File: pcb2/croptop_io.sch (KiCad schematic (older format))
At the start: 162 parts, among them J10 1702474, J11 1702474, J12 1702474, J13 1702474, J14 1702474, J7 1702474, J8 1702474, J9 1702474, Q3 FDMA530PZ, U18 AP22802AW5, U19 74HCT125D653, U20 AP22802AW5, U21 AD7799, U22 TPD4E1U06DBV, U23 AP22802AW5, U24 TPD4E1U06DBV, U25 TPD4E1U06DBV, U26 TPD4E1U06DBV, U27 DRV8872, U28 DRV8825, U29 AP22802AW5

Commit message: Footprints done, board started
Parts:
- removed D13, D14, D17, D19: LTSTC171GKT, LED_SMD:LED_0805_2012Metric, symbol Device:LED
- removed JP1: N.0., symbol Jumper:SolderJumper_2_Open
- removed Q3: FDMA530PZ, symbol Device:Q_PMOS_DGS
- removed R100, R94, R95, R96: 110m, symbol Device:R
- removed R60, R68, R73, R93: 10k, Resistor_SMD:R_0402_1005Metric, symbol Device:R
- removed R70, R72, R99: 100, Resistor_SMD:R_0402_1005Metric, symbol Device:R
- removed R71: 0, Resistor_SMD:R_0402_1005Metric, symbol Device:R
- removed R75: 220, Resistor_SMD:R_0402_1005Metric, symbol Device:R
- removed TP59, TP60, TP63, TP95: TestPoint, symbol Connector:TestPoint
- added C74, C76: 0.1u, Capacitor_SMD:C_0402_1005Metric, symbol Device:C
- added JP1: Solder Jumper, Jumper:SolderJumper-3_P1.3mm_Bridged12_RoundedPad1.0x1.5mm, symbol Jumper:SolderJumper_3_Bridged12
- added Q3: Q2319ADS-T1-GE3, Package_TO_SOT_SMD:SOT-23, symbol Device:Q_PMOS_GSD
- added R83, R84, R88: 0.2, Resistor_SMD:R_2512_6332Metric, symbol Device:R
- C45: renamed from C46; footprint Capacitor_SMD:C_0402_1005Metric -> Capacitor_SMD:C_1206_3216Metric
- C46: renamed from C47; footprint Capacitor_SMD:C_0402_1005Metric -> Capacitor_SMD:C_1206_3216Metric
- C47: renamed from C45; footprint Capacitor_SMD:C_0402_1005Metric -> Capacitor_SMD:C_1206_3216Metric
- C48, C51, C52, C56, C58, C61, C62: footprint Capacitor_SMD:C_0402_1005Metric -> Capacitor_SMD:C_1206_3216Metric
- C66: renamed from C67; value 0.1u -> 0.01u; MPN (none) -> CL05B103KB5NNNC; Rating (none) -> 50V
- C67: renamed from C66; footprint Capacitor_SMD:C_0402_1005Metric -> Capacitor_SMD:C_1206_3216Metric
- C68, C71: footprint Capacitor_SMD:C_0402_1005Metric -> Capacitor_SMD:C_0805_2012Metric; Rating (none) -> 50V
- C69: renamed from C70; Rating (none) -> 50V
- C70: renamed from C69; footprint Capacitor_SMD:C_0402_1005Metric -> Capacitor_SMD:C_0805_2012Metric
- C72: Rating (none) -> 35V
- C75: renamed from C74; footprint Capacitor_SMD:C_0402_1005Metric -> Capacitor_SMD:C_1206_3216Metric
- D12: renamed from D15; footprint (none) -> Diode_SMD:D_0201_0603Metric
- D13: renamed from D16; footprint (none) -> Diode_SMD:D_0201_0603Metric
- D14: renamed from D18; footprint (none) -> Diode_SMD:D_0201_0603Metric
- D15: renamed from D20; footprint (none) -> Diode_SMD:D_SMA
- D16: renamed from D21; footprint (none) -> Diode_SMD:D_0201_0603Metric
- D17: renamed from D22; footprint (none) -> Package_TO_SOT_SMD:SOT-323_SC-70
- D18: renamed from D23; footprint (none) -> Package_TO_SOT_SMD:SOT-323_SC-70
- D19: renamed from D24; footprint (none) -> Package_TO_SOT_SMD:SOT-323_SC-70
- D20: renamed from D25; footprint (none) -> Package_TO_SOT_SMD:SOT-323_SC-70
- J10, J11, J12, J13, J14, J7, J8, J9: footprint (none) -> croptop:solderless_terminal
- L4: footprint (none) -> Inductor_SMD:L_0402_1005Metric
- R85: renamed from R98; footprint (none) -> Resistor_SMD:R_0402_1005Metric
- R89: renamed from R101; value 110m -> 0.2; footprint (none) -> Resistor_SMD:R_2512_6332Metric; MPN (none) -> CSRN2512FKR200
- TP50: renamed from TP53; footprint (none) -> croptop:TestPoint
- TP51: renamed from TP54; footprint (none) -> croptop:TestPoint
- TP52: renamed from TP55; footprint (none) -> croptop:TestPoint
- TP53: renamed from TP56; footprint (none) -> croptop:TestPoint
- TP54: renamed from TP57; footprint (none) -> croptop:TestPoint
- TP55: renamed from TP58; footprint (none) -> croptop:TestPoint
- TP56: renamed from TP61; footprint (none) -> croptop:TestPoint
- TP58: renamed from TP64; footprint (none) -> croptop:TestPoint
- TP59: renamed from TP65; footprint (none) -> croptop:TestPoint
- TP60: renamed from TP66; footprint (none) -> croptop:TestPoint
- TP61: renamed from TP67; footprint (none) -> croptop:TestPoint
- TP62: renamed from TP68; footprint (none) -> croptop:TestPoint
- TP63: renamed from TP69; footprint (none) -> croptop:TestPoint
- TP64: renamed from TP70; footprint (none) -> croptop:TestPoint
- TP65: renamed from TP71; footprint (none) -> croptop:TestPoint
- TP66: renamed from TP72; footprint (none) -> croptop:TestPoint
- TP67: renamed from TP73; footprint (none) -> croptop:TestPoint
- TP68: renamed from TP62; footprint (none) -> croptop:TestPoint
- TP69: renamed from TP74; footprint (none) -> croptop:TestPoint
- TP70: renamed from TP75; footprint (none) -> croptop:TestPoint
- TP71: renamed from TP76; footprint (none) -> croptop:TestPoint
- TP72: renamed from TP77; footprint (none) -> croptop:TestPoint
- TP73: renamed from TP78; footprint (none) -> croptop:TestPoint
- TP74: renamed from TP79; footprint (none) -> croptop:TestPoint
- TP75: renamed from TP80; footprint (none) -> croptop:TestPoint
- TP76: renamed from TP81; footprint (none) -> croptop:TestPoint
- TP77: renamed from TP82; footprint (none) -> croptop:TestPoint
- TP78: renamed from TP83; footprint (none) -> croptop:TestPoint
- TP79: renamed from TP84; footprint (none) -> croptop:TestPoint
- TP80: renamed from TP85; footprint (none) -> croptop:TestPoint
- TP81: renamed from TP86; footprint (none) -> croptop:TestPoint
- TP82: renamed from TP87; footprint (none) -> croptop:TestPoint
- TP83: renamed from TP88; footprint (none) -> croptop:TestPoint
- TP84: renamed from TP89; footprint (none) -> croptop:TestPoint
- TP85: renamed from TP90; footprint (none) -> croptop:TestPoint
- TP86: renamed from TP91; footprint (none) -> croptop:TestPoint
- TP87: renamed from TP92; footprint (none) -> croptop:TestPoint
- TP88: renamed from TP93; footprint (none) -> croptop:TestPoint
- TP89: renamed from TP94; footprint (none) -> croptop:TestPoint
- TP90: renamed from TP96; footprint (none) -> croptop:TestPoint
- TP91: renamed from TP97; footprint (none) -> croptop:TestPoint
- TP92: renamed from TP98; footprint (none) -> croptop:TestPoint
- TP93: renamed from TP100; footprint (none) -> croptop:TestPoint
- TP94: renamed from TP99; footprint (none) -> croptop:TestPoint
- TP95: renamed from TP101; footprint (none) -> croptop:TestPoint
- TP96: renamed from TP102; footprint (none) -> croptop:TestPoint
- TP97: renamed from TP103; footprint (none) -> croptop:TestPoint
- TP98: renamed from TP104; footprint (none) -> croptop:TestPoint
- U19: renamed from U18; footprint (none) -> Package_TO_SOT_SMD:SOT-23-5
- U21: renamed from U20; footprint (none) -> Package_TO_SOT_SMD:SOT-23-5
- U23, U29: footprint (none) -> Package_TO_SOT_SMD:SOT-23-5
- renumbered C75 to C77, R61 to R55, R62 to R56, R64 to R57, R65 to R58, R66 to R59, R67 to R60, R63 to R61, R69 to R62, R74 to R65, R76 to R66, R77 to R67, R78 to R68, R79 to R69, R80 to R70, R81 to R71, R82 to R72, R83 to R73, R84 to R74, R85 to R75, R86 to R76, R87 to R77, R88 to R78, R89 to R79, R90 to R80, R91 to R81, R92 to R82, R97 to R86, R102 to R87, U19 to U18, U21 to U20
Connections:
- net ~ENCDR_PWR_FAULT is gone; now on net ~PWR_FAULT: U23.3 (FLG)
- net ~POTEN_PWR_FAULT is gone; now on net ~PWR_FAULT: U19.3 (FLG)
- net ~SONIC_PWR_FAULT is gone; now on net ~PWR_FAULT: U21.3 (FLG)
- net +3V3: now also JP1.3 (B)
- net +5V: now also JP1.1 (A)
- net DGND: now also C74.2, C76.2, R83.2, R84.2, R88.2
- net at C68.1, C69.2, C70.1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: now also Q3.2 (S)
- net at U27.7 (ISEN): now also R83.1, R84.1
- net at C73.1, U28.12 (AVREF), U28.13 (BVREF)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: now also C74.1, C76.1
- net at U28.9 (ISENB): now also R88.1
- net at C51.1, R65.1, U23.4 (EN)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: now also JP1.2 (C)
- net at D18.1 (A1), D18.2 (A2), J13.3 (Pin_3): now also Q3.3 (D)
- net at D15.2 (A), R87.1: now also Q3.1 (G)
- net ~ADI_PWR_FAULT renamed ~PWR_FAULT
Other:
- note added: "Scratch 1-2 connection\nand solder 3-2 connection\nfor 3.3V encoders"
- note removed: "RL1220S-R11"
- note removed: "Remove resistor \nif using jumper"
- moved on the sheet: C47, C48, C67, C70, C71, C73, R61, R62, R86, R89, TP56, TP68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

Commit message: Updated prez
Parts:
- U18: footprint (none) -> Package_SO:SOIC-14_3.9x8.7mm_P1.27mm
- U22, U24, U25, U26: footprint (none) -> Package_TO_SOT_SMD:SOT-23-6
- U28: footprint (none) -> Package_SO:HTSSOP-28-1EP_4.4x9.7mm_P0.65mm_EP3.4x9.5mm_Mask2.4x6.17mm_ThermalVias
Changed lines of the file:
@@
 F 0 "U25" H 8850 3426 50  0000 C CNN
 F 1 "TPD4E1U06DBV" H 8850 3335 50  0000 C CNN
-F 2 "" V 9100 3100 50  0001 C CNN
+F 2 "Package_TO_SOT_SMD:SOT-23-6" V 9100 3100 50  0001 C CNN
 F 3 "http://www.ti.com/lit/ds/symlink/tpd4e1u06.pdf" V 9100 3100 50  0001 C CNN
 	1    8850 3650
@@
 F 0 "U26" H 9750 3426 50  0000 C CNN
 F 1 "TPD4E1U06DBV" H 9750 3335 50  0000 C CNN
-F 2 "" V 10000 3100 50  0001 C CNN
+F 2 "Package_TO_SOT_SMD:SOT-23-6" V 10000 3100 50  0001 C CNN
 F 3 "http://www.ti.com/lit/ds/symlink/tpd4e1u06.pdf" V 10000 3100 50  0001 C CNN
 	1    9750 3650
@@
 F 0 "U18" H 2150 9500 50  0000 C CNN
 F 1 "74HCT125D653" H 2150 9400 50  0000 C CNN
-F 2 "" H 3500 9250 50  0001 C CNN
+F 2 "Package_SO:SOIC-14_3.9x8.7mm_P1.27mm" H 3500 9250 50  0001 C CNN
 F 3 "https://assets.nexperia.com/documents/data-sheet/74HC_HCT125.pdf" H 3500 9250 50  0001 C CNN
 	1    2450 9250
@@
 F 0 "U22" H 3550 9726 50  0000 C CNN
 F 1 "TPD4E1U06DBV" H 3550 9635 50  0000 C CNN
-F 2 "" V 3800 9400 50  0001 C CNN
+F 2 "Package_TO_SOT_SMD:SOT-23-6" V 3800 9400 50  0001 C CNN
 F 3 "http://www.ti.com/lit/ds/symlink/tpd4e1u06.pdf" V 3800 9400 50  0001 C CNN
 	1    3550 9950
@@
 F 0 "U28" H 11400 8800 50  0000 C CNN
 F 1 "DRV8825" H 11400 8700 50  0000 C CNN
-F 2 "" H 11150 8550 50  0001 C CNN
+F 2 "Package_SO:HTSSOP-28-1EP_4.4x9.7mm_P0.65mm_EP3.4x9.5mm_Mask2.4x6.17mm_ThermalVias" H 11150 8550 50  0001 C CNN
 F 3 "http://www.ti.com/lit/ds/symlink/drv8825.pdf" H 11150 8550 50  0001 C CNN
 	1    11150 8050
@@
 F 0 "U24" H 6350 7376 50  0000 C CNN
 F 1 "TPD4E1U06DBV" H 6350 7285 50  0000 C CNN
-F 2 "" V 6600 7050 50  0001 C CNN
+F 2 "Package_TO_SOT_SMD:SOT-23-6" V 6600 7050 50  0001 C CNN
 F 3 "http://www.ti.com/lit/ds/symlink/tpd4e1u06.pdf" V 6600 7050 50  0001 C CNN
 	1    6350 7600

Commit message: Board almost done
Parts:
- removed TP70, TP71, TP73, TP77, TP79, TP83: TestPoint, croptop:TestPoint, symbol Connector:TestPoint
- renumbered C67 to C66, C66 to C67, C75 to C72, C72 to C73, C73 to C74, C77 to C75, C74 to C76, C76 to C77, R65 to R63, R66 to R64, R67 to R65, R68 to R66, R69 to R67, R70 to R68, R71 to R69, R72 to R70, R73 to R71, R74 to R72, R75 to R73, R76 to R74, R77 to R75, R78 to R76, R79 to R77, R80 to R78, R81 to R79, R82 to R80, R86 to R81, R83 to R82, R84 to R83, R85 to R84, R87 to R85, R88 to R86, R89 to R87, TP50 to TP16, TP51 to TP17, TP52 to TP18, TP53 to TP19, TP54 to TP20, TP55 to TP21, TP56 to TP22, TP58 to TP23, TP59 to TP24, TP60 to TP25, TP61 to TP26, TP62 to TP27, TP63 to TP28, TP64 to TP29, TP65 to TP30, TP66 to TP31, TP67 to TP32, TP68 to TP33, TP69 to TP34, TP72 to TP35, TP74 to TP36, TP75 to TP37, TP76 to TP38, TP78 to TP39, TP80 to TP40, TP81 to TP41, TP82 to TP42, TP84 to TP43, TP85 to TP44, TP86 to TP45, TP87 to TP46, TP88 to TP47, TP89 to TP48, TP90 to TP49, TP91 to TP50, TP92 to TP51, TP94 to TP52, TP93 to TP53, TP95 to TP54, TP96 to TP55, TP97 to TP56, TP98 to TP57
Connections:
- net ENCDR_A: now also R56.2, TP16.1; no longer R55.2, TP17.1
- net ENCDR_B: now also R55.2, TP17.1; no longer R56.2, TP16.1
- net at D17.2 (A2), TP51.1, U27.6 (OUT1): now also J13.2 (Pin_2); no longer J13.1 (Pin_1)
- net at D17.1 (A1), TP50.1, U27.8 (OUT2): now also J13.1 (Pin_1); no longer J13.2 (Pin_2)
- net at R64.2, U22.6 (D1-): now also U18.5 (A2); no longer U18.2 (A1)
- net at R65.2, U22.1 (D1+): now also U18.2 (A1); no longer U18.5 (A2)
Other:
- moved on the sheet: C66, C72, C75, D16, J10, J11, J12, R81, TP52, U29

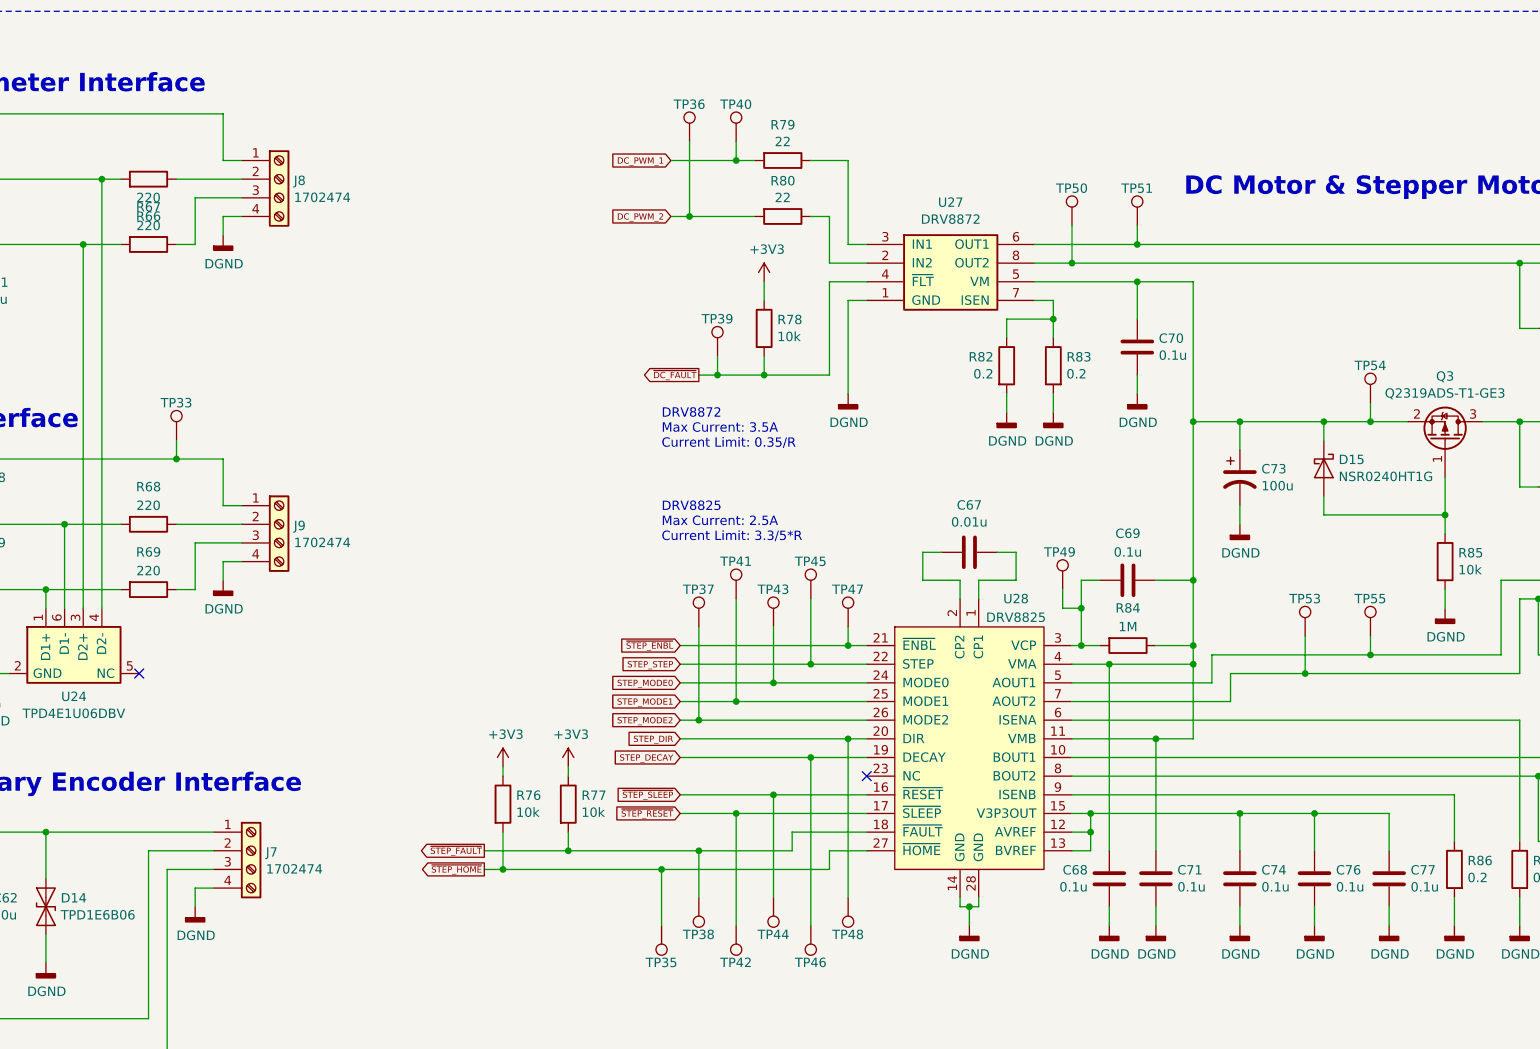
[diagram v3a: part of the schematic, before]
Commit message: Updated PCB2, Changed MotorLib, Changed PotLib
- Updated PCB2 to have all correct MPNs
- Added some useful macros within the standard hardware heade file
- Changed hardware initialization function calls (for main, MotorLib, and PotLib) to return an error flag.
- Corrected GPIO configurations for switches, LEDS
- Made initialize_system() private
- Added Doxygen to MotorLib and PotLib files
- Reduced bloat of MotorLib by combining subsystem setup functions into one.
- Added boundary condition checks for PWM functions
- Added error-flag return values to motor functions
- Corrected issue where CN14 was "used" to detect faults, but in PCBv2.2 CN14 is connected to GPU_INT, and INT1 is connected to DC_FAULT. Updated code accordingly.
- Made ADC / Potentiometer functionality "smart" configure T3 to sample the ADC at a variable, desired frequency.
- Updated potentiometer configuration to use AN9 and AN10
- Added error-flag returns to initialize_potentiometer()
- Added ISR for timer 3 that is used to trigger ADC samples automatically
- Added multi-inclusion protection to all currently-addressed files (will do rest later)

** THIS HAS NOT BEEN COMPILE VERIFIED - CHECK WITH XC32 COMPILER **
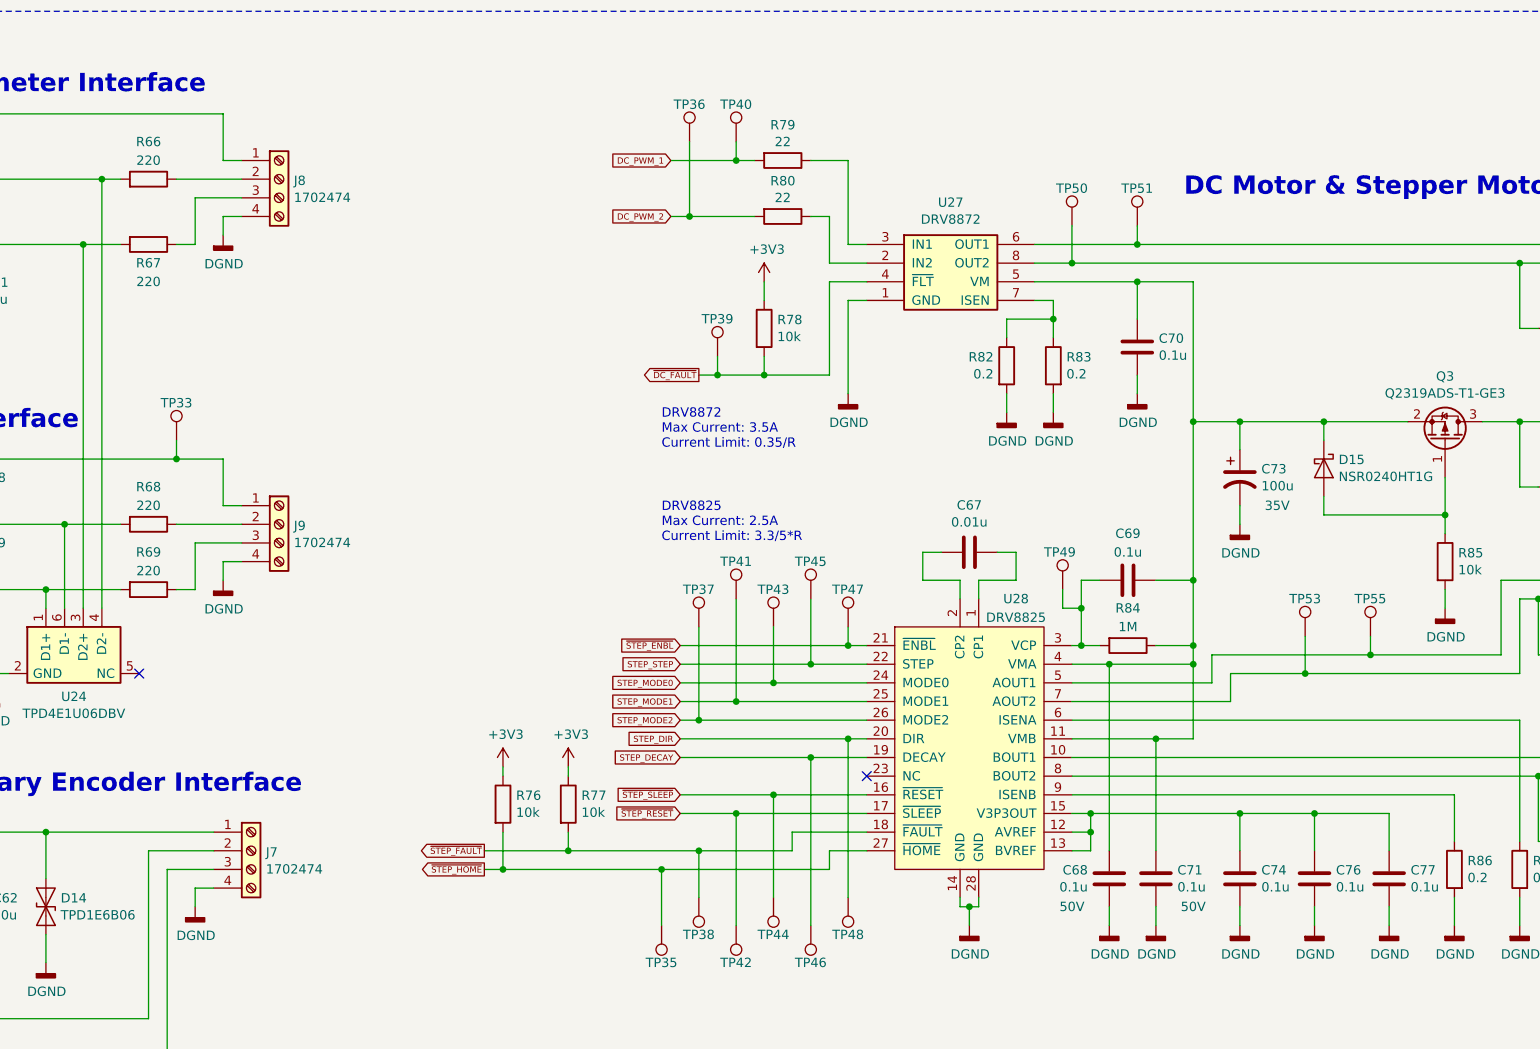
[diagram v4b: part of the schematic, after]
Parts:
- removed TP54: TestPoint, croptop:TestPoint, symbol Connector:TestPoint
- C45, C46, C47, C48, C51, C52, C56, C58, C61, C62, C66, C72: MPN (none) -> CC1206ZRY5V6BB106
- C49, C50, C53, C54, C55, C57, C59, C60, C63, C64, C65, C69, C74, C75, C76, C77: MPN (none) -> CL05F104ZO5NNNC
- C67: MPN CL05B103KB5NNNC -> CC0402KRX7R9BB103
- C68, C70, C71: MPN (none) -> C0805C104Z5VACTU
- C73: MPN (none) -> UWT1V101MCL1GS
- D12, D13, D14, D16: MPN (none) -> TPD1E6B06DPLR
- D15: footprint Diode_SMD:D_SMA -> Diode_SMD:D_SOD-323; MPN (none) -> NSR0240HT1G
- D17, D18, D19, D20: MPN (none) -> TPD2E007DCKR
- J10, J11, J12, J13, J14, J7, J8, J9: MPN (none) -> 277-2338-1-ND
- JP1: MPN (none) -> JL-100-25-T
- L4: MPN (none) -> BKP1005HS121-TV
- Q3: MPN (none) -> SQ2319ADS-T1_GE3
- R55, R56, R57, R58, R59, R60, R79, R80: MPN (none) -> RC0402FR-0722RL
- R61, R62, R63, R76, R77, R78, R81, R85: MPN (none) -> RC0402FR-0710KL
- R64, R65, R66, R67, R68, R69: MPN (none) -> CRGCQ0402F220R
- R70, R71, R72, R73, R74, R75: MPN (none) -> RC0402FR-07100RL
- R84: MPN (none) -> RC0402FR-071ML
- TP16, TP17, TP18, TP19, TP20, TP21, TP22, TP23, TP24, TP25, TP26, TP27, TP28, TP29, TP30, TP31, TP32, TP33, TP34, TP35, TP36, TP37, TP38, TP39, TP40, TP41, TP42, TP43, TP44, TP45, TP46, TP47, TP48, TP49, TP50, TP51, TP52, TP53, TP55, TP56, TP57: footprint croptop:TestPoint -> TestPoint:TestPoint_Pad_D1.0mm
- U18: MPN (none) -> 74HCT125D,653
- U19, U21, U23, U29: MPN (none) -> AP22802AW5-7
- U20: MPN (none) -> AD7799BRUZ
- U22, U24, U25, U26: MPN (none) -> TPD4E1U06DBVR
- U27: MPN (none) -> DRV8872DDAR
- U28: MPN (none) -> DRV8825PWPR
